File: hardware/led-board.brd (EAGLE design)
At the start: 100 x 15.3 mm, 22 parts, among them U1 ATMEGA168PA-AU

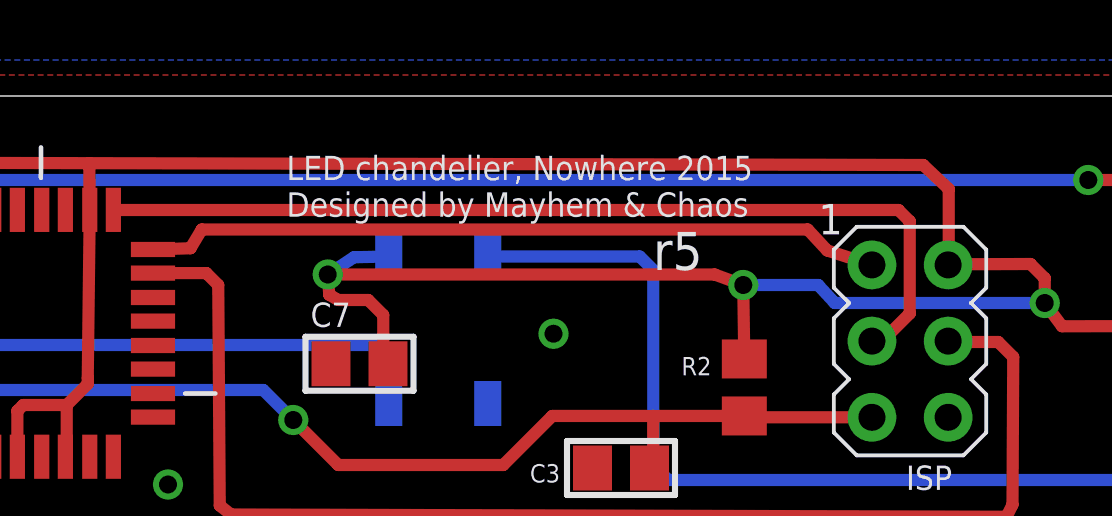
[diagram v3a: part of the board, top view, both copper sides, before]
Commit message: Ported code to aduino and it looks like everything should fit!!!
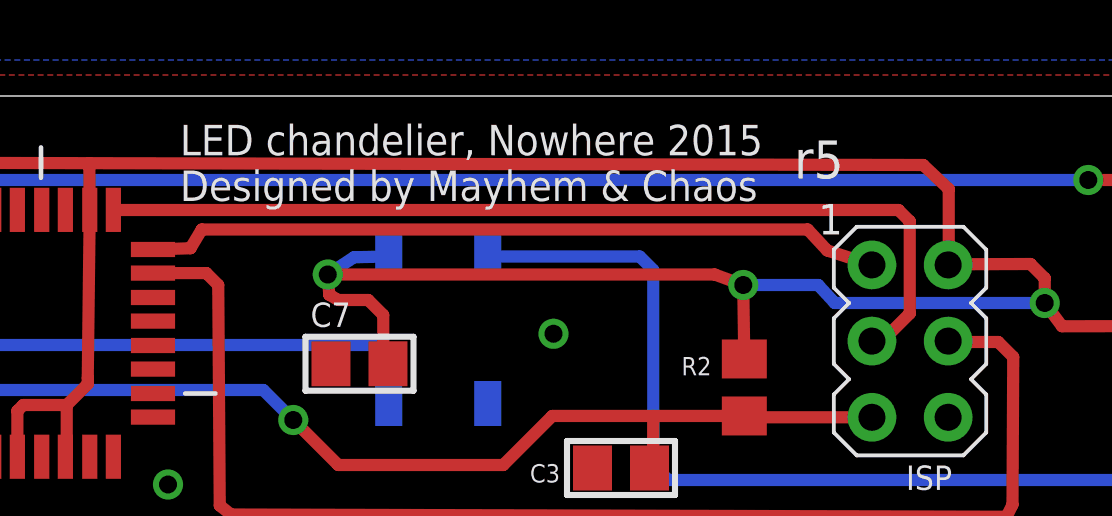
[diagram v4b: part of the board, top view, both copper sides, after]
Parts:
- R1: value 300 -> 330
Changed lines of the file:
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@@
 <layer number="21" name="tPlace" color="7" fill="1" visible="yes" active="yes"/>
 <layer number="22" name="bPlace" color="7" fill="1" visible="yes" active="yes"/>
-<layer number="23" name="tOrigins" color="15" fill="1" visible="yes" active="yes"/>
-<layer number="24" name="bOrigins" color="15" fill="1" visible="yes" active="yes"/>
+<layer number="23" name="tOrigins" color="15" fill="1" visible="no" active="yes"/>
+<layer number="24" name="bOrigins" color="15" fill="1" visible="no" active="yes"/>
 <layer number="25" name="tNames" color="7" fill="1" visible="yes" active="yes"/>
 <layer number="26" name="bNames" color="7" fill="1" visible="yes" active="yes"/>
@@
 <text x="10.925" y="6.275" size="0.6096" layer="25">RX</text>
 <text x="25.275" y="9.55" size="0.8128" layer="25">VCC</text>
-<text x="60.275" y="11.275" size="0.8128" layer="25">LED chandelier, Nowhere 2015
+<text x="56.725" y="11.8" size="1.016" layer="25">LED chandelier, Nowhere 2015
 Designed by Mayhem &amp; Chaos</text>
-<text x="72.5" y="9.5" size="1.27" layer="25">r5</text>
+<text x="77.2" y="12.55" size="1.27" layer="25">r5</text>
 <hole x="11.5" y="13.3" drill="2.8"/>
 <hole x="11.5" y="2" drill="2.8"/>
@@
 <attribute name="MPN" value="WS2812B" x="34.666" y="7.5" size="1.778" layer="27" rot="R90" display="off"/>
 </element>
-<element name="R1" library="resistor" package="R0805" value="300" x="22.35" y="3.25" smashed="yes" rot="R180">
+<element name="R1" library="resistor" package="R0805" value="330" x="22.35" y="3.25" smashed="yes" rot="R180">
 <attribute name="NAME" x="24.085" y="2.105" size="0.6096" layer="25" rot="R180"/>
-<attribute name="OC_NEWARK" value="58K4799" x="22.35" y="3.25" size="1.778" layer="27" rot="R180" display="off"/>
-<attribute name="MF" value="Multicomp Passives" x="22.35" y="3.25" size="1.778" layer="27" rot="R180" display="off"/>
-<attribute name="MPN" value="MC01W08051300R" x="22.35" y="3.25" size="1.778" layer="27" rot="R180" display="off"/>
+<attribute name="OC_NEWARK" value="66R3661" x="22.35" y="3.25" size="1.778" layer="27" rot="R180" display="off"/>
+<attribute name="MF" value="" x="22.35" y="3.25" size="1.778" layer="27" rot="R180" display="off"/>
+<attribute name="MPN" value="RC0805JR-07330RL" x="22.35" y="3.25" size="1.778" layer="27" rot="R180" display="off"/>
 </element>
 <element name="R2" library="resistor" package="R0805" value="10k" x="75.535" y="5.585" smashed="yes" rot="R90">
